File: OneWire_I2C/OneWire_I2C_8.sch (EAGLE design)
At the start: 21 parts, among them U1 P82B715D

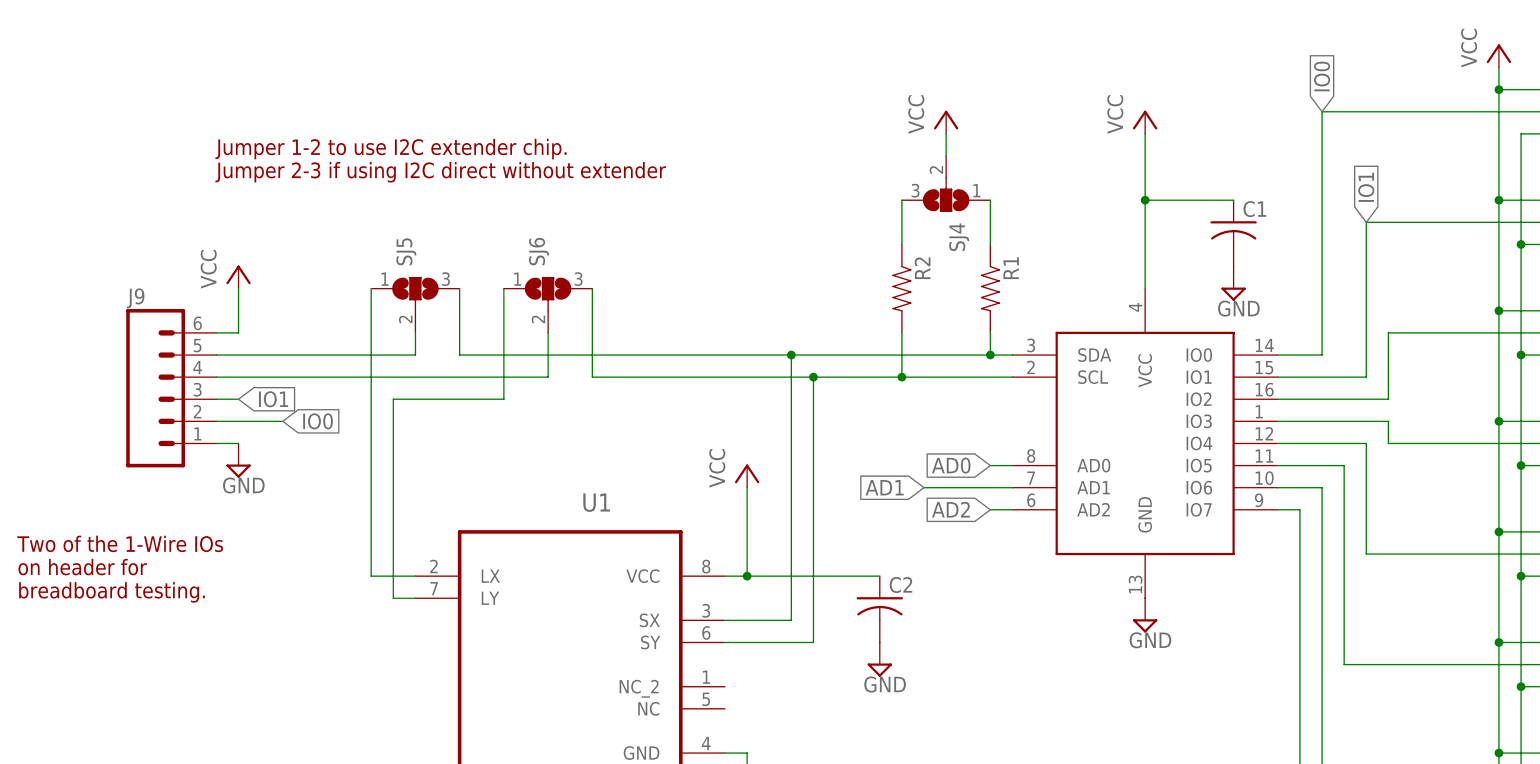
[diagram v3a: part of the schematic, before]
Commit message: Enlarged board, added regulator, replaced header with push connectors
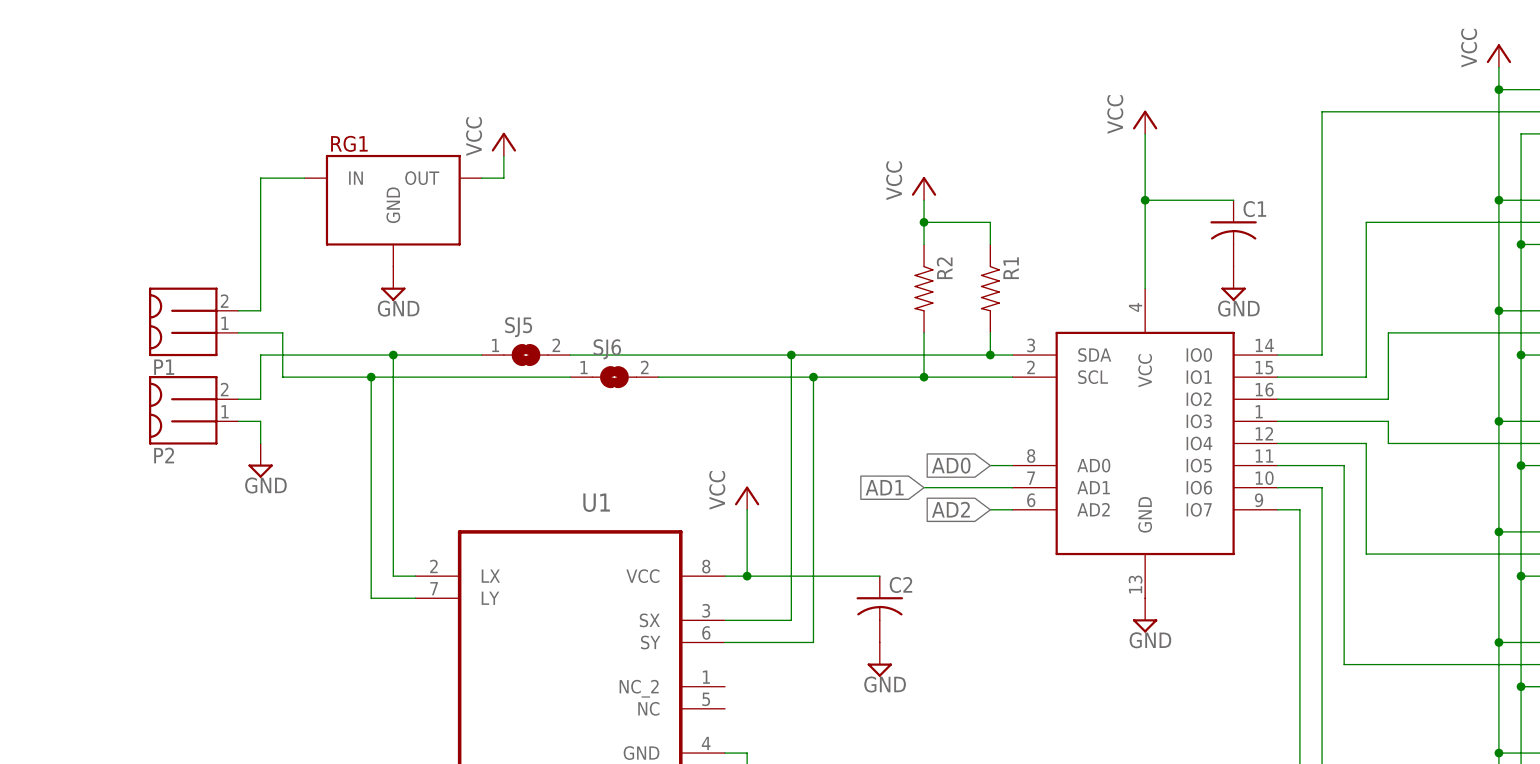
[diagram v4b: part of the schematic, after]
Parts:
- removed J9: (no value), SparkFun-Connectors:M06SILK_FEMALE_PTH
- removed SJ4: (no value), jumper:SJ2W
- added P1, P2: MOLEX_MINILITE_TRAP_2, Puffin:MOLEX_MINILITE_TRAP_2
- added RG1: (no value), Puffin:MURATA_REG
- SJ5, SJ6: device jumper:SJ2W -> jumper:SJ
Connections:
- removed net LSCL: J9.4, SJ6.2
- removed net LSDA: J9.5, SJ5.2
- removed net LX: SJ5.1, U1.LX
- removed net N$1: R2.1, SJ4.3
- removed net N$2: R1.1, SJ4.1
- new net IN: P1.2, RG1.IN
- new net N$3: P2.2, SJ5.1, U1.LX
- net GND: now also P2.1, RG1.GND; no longer J9.1
- net IO0: no longer J9.2
- net IO1: no longer J9.3
- net LY: now also P1.1
- net SCL: now also SJ6.2; no longer SJ6.3
- net SDA: now also SJ5.2; no longer SJ5.3
- net VCC: now also R1.1, R2.1, RG1.OUT; no longer J9.6, SJ4.2
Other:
- note removed: "Jumper 1-2 to use I2C extender chip. Jumper 2-3 if using I2C direct without extender"
- note removed: "Two of the 1-Wire IOs on header for breadboard testing."
- moved on the sheet: R2
